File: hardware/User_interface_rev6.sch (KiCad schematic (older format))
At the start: 42 parts, among them IC201 CAT4002ATD-GT3, SW201 F1, SW202 F4, SW203 F7, SW204 ESTOP, SW205 F0, SW206 F2, SW207 F5, SW208 F8, SW209 LOCO1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

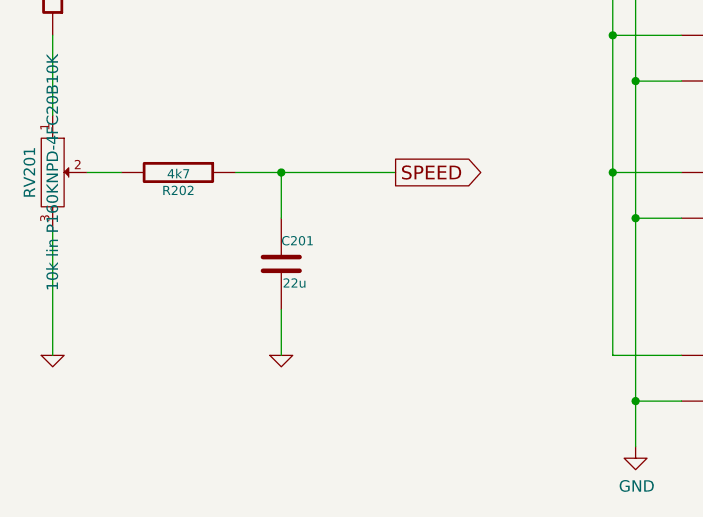
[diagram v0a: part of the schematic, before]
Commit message: Decrease poti lowpass cap to 4u7
Faster speed response
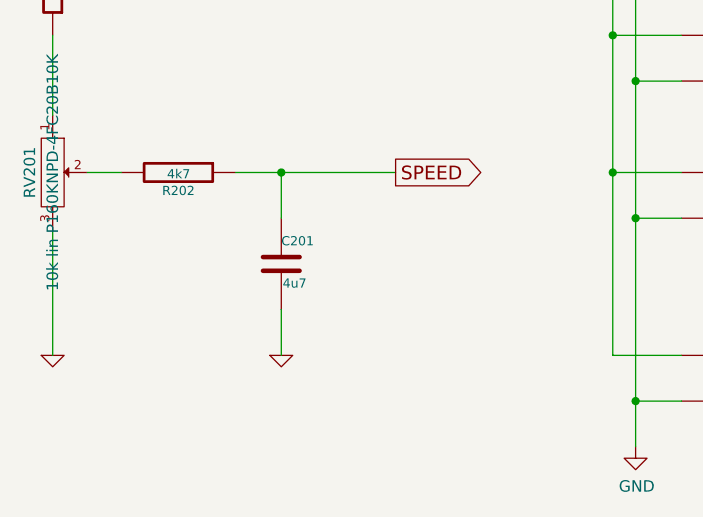
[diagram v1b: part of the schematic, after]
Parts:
- C201: value 22u -> 4u7; LCSC C45783 -> C1779; Mouser 187-CL21A226MAYNNNE -> (none); Reichelt KEM X5R0805 22U -> KEM X5R0805 4,7U; Remark Mouser 25V, LCSC/Reichelt 6V3 -> (none)
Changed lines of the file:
@@
 Wire Wire Line
 	1150 5250 1300 5250
-$Comp
-L wfred_rev6-rescue:C-RESCUE-wfred_rev2-wfred_rev2-rescue C201
-U 1 1 59210B2F
-P 2000 5650
-AR Path="/59210B2F" Ref="C201"  Part="1"
-AR Path="/5920DD4A/59210B2F" Ref="C201"  Part="1"
-F 0 "C201" H 2000 5750 40  0000 L CNN
-F 1 "22u" H 2006 5565 40  0000 L CNN
-F 2 "Capacitor_SMD:C_0805_2012Metric_Pad1.15x1.40mm_HandSolder" H 2038 5500 30  0001 C CNN
-F 3 "" H 2000 5650 60  0000 C CNN
-F 4 "KEM X5R0805 22U" H 2000 5650 60  0001 C CNN "Reichelt"
-F 5 "C45783" H 2000 5650 50  0001 C CNN "LCSC"
-F 6 "187-CL21A226MAYNNNE" H 2000 5650 50  0001 C CNN "Mouser"
-F 7 "Mouser 25V, LCSC/Reichelt 6V3" H 2000 5650 50  0001 C CNN "Remark"
-	1    2000 5650
-	1    0    0    -1
-$EndComp
 Wire Wire Line
 	1800 5250 2000 5250
@@
 Wire Wire Line
 	6650 5750 6650 5650
+$Comp
+L wfred_rev6-rescue:C-RESCUE-wfred_rev2-wfred_rev2-rescue C?
+U 1 1 60C635A2
+P 2000 5650
+AR Path="/60C635A2" Ref="C?"  Part="1"
+AR Path="/5920DD4A/60C635A2" Ref="C201"  Part="1"
+F 0 "C201" H 2000 5750 40  0000 L CNN
+F 1 "4u7" H 2006 5565 40  0000 L CNN
+F 2 "Capacitor_SMD:C_0805_2012Metric_Pad1.15x1.40mm_HandSolder" H 2038 5500 30  0001 C CNN
+F 3 "" H 2000 5650 60  0000 C CNN
+F 4 "KEM X5R0805 4,7U" H 2000 5650 60  0001 C CNN "Reichelt"
+F 5 "C1779" H 2000 5650 50  0001 C CNN "LCSC"
+	1    2000 5650
+	1    0    0    -1
+$EndComp
 $EndSCHEMATC

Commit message: Update BAT54C order number...
...to one in stock at LCSC
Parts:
- D201, D202, D203, D204: LCSC C375703 -> C556168
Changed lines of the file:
@@
 F 2 "Package_TO_SOT_SMD:SOT-23" H 5925 4475 50  0001 L CNN
 F 3 "http://www.diodes.com/_files/datasheets/ds11005.pdf" H 5770 4350 50  0001 C CNN
-F 4 "C375703" V 5850 4350 50  0001 C CNN "LCSC"
+F 4 "C556168" V 5850 4350 50  0001 C CNN "LCSC"
 F 5 "BAT 54C NXP" V 5850 4350 50  0001 C CNN "Reichelt"
 F 6 "583-BAT54C" V 5850 4350 50  0001 C CNN "Mouser"
@@
 F 2 "Package_TO_SOT_SMD:SOT-23" H 5925 5875 50  0001 L CNN
 F 3 "http://www.diodes.com/_files/datasheets/ds11005.pdf" H 5770 5750 50  0001 C CNN
-F 4 "C375703" V 5850 5750 50  0001 C CNN "LCSC"
+F 4 "C556168" V 5850 5750 50  0001 C CNN "LCSC"
 F 5 "BAT 54C NXP" V 5850 5750 50  0001 C CNN "Reichelt"
 F 6 "583-BAT54C" V 5850 5750 50  0001 C CNN "Mouser"
@@
 F 2 "Package_TO_SOT_SMD:SOT-23" H 4925 4475 50  0001 L CNN
 F 3 "http://www.diodes.com/_files/datasheets/ds11005.pdf" H 4770 4350 50  0001 C CNN
-F 4 "C375703" V 4850 4350 50  0001 C CNN "LCSC"
+F 4 "C556168" V 4850 4350 50  0001 C CNN "LCSC"
 F 5 "BAT 54C NXP" V 4850 4350 50  0001 C CNN "Reichelt"
 F 6 "583-BAT54C" V 4850 4350 50  0001 C CNN "Mouser"
@@
 F 2 "Package_TO_SOT_SMD:SOT-23" H 4925 5875 50  0001 L CNN
 F 3 "http://www.diodes.com/_files/datasheets/ds11005.pdf" H 4770 5750 50  0001 C CNN
-F 4 "C375703" V 4850 5750 50  0001 C CNN "LCSC"
+F 4 "C556168" V 4850 5750 50  0001 C CNN "LCSC"
 F 5 "BAT 54C NXP" V 4850 5750 50  0001 C CNN "Reichelt"
 F 6 "583-BAT54C" V 4850 5750 50  0001 C CNN "Mouser"
